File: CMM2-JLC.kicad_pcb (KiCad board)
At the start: 4 copper layers, 130 x 102 mm, 112 parts, among them J1 Nunchuck, J2 VGA, J3 EXTERNAL I/O, J4 USB_C_Receptacle_USB2.0, J5 Audio, J6 USB A Host, J7 SWD, J8 Micro_SD_Card_Det, J9 Boot select, SW1 Reset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

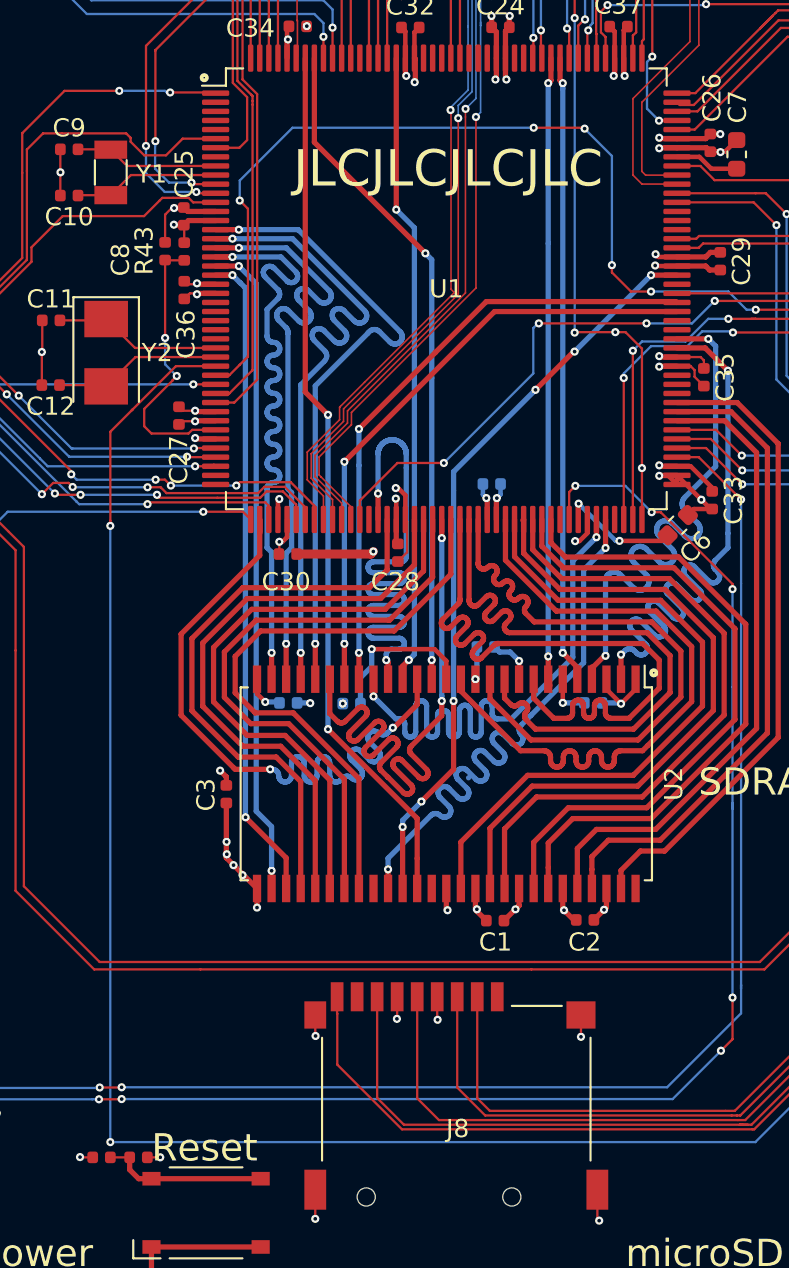
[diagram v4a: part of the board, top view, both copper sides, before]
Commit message: Fix reversed SDRAM bank select and some style/DRC issues
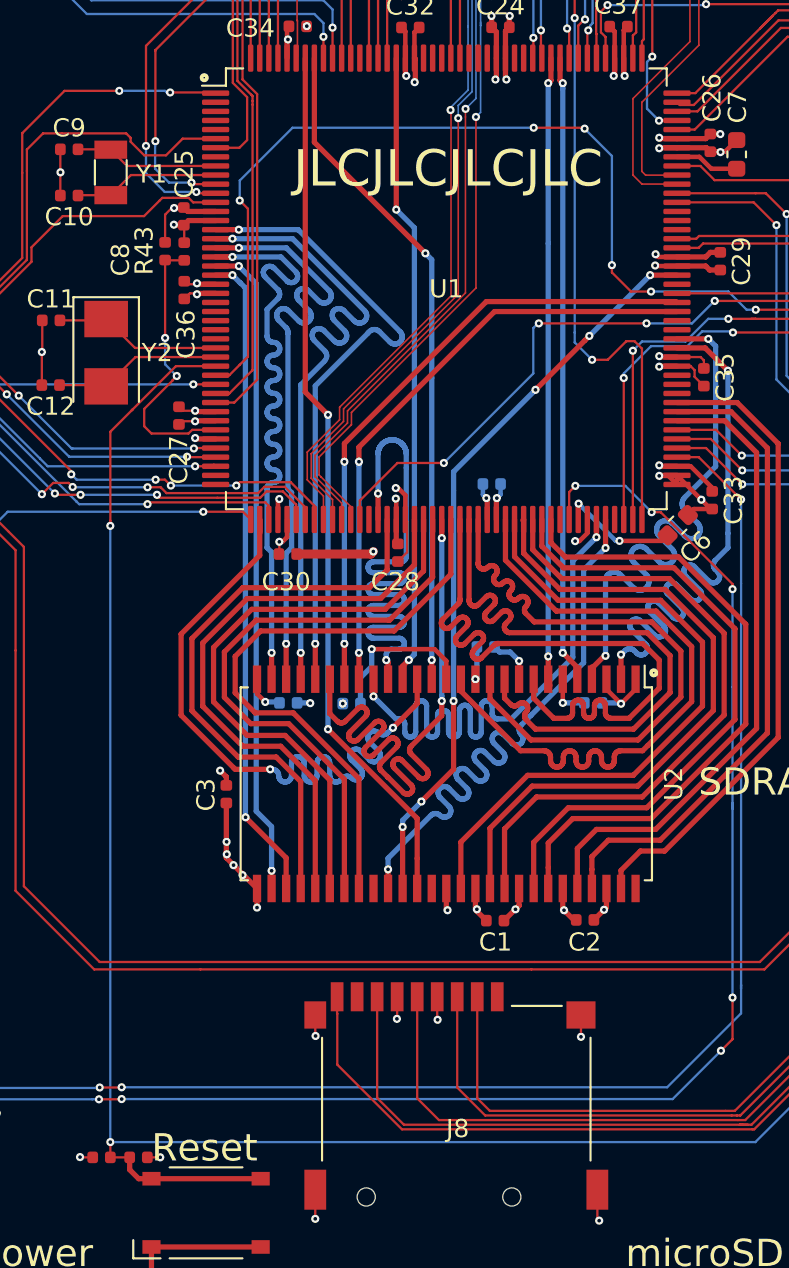
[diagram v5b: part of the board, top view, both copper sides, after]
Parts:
- removed REF**: OSHW-Logo_38.1x40mm_SilkScreen, Symbol:OSHW-Logo_38.1x40mm_SilkScreen
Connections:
- U2 pad 20: /PG5 -> /PG4
- U2 pad 21: /PG4 -> /PG5
- U3 pad 1: /USB_C_D+ -> /USB_C_D-
- U3 pad 3: /USB_C_D- -> /USB_C_D+
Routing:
- net /I2C2_SCL: track 61.4 -> 62.6 mm, vias 6 -> 4
- net /RESET: track 151.1 -> 151.9 mm

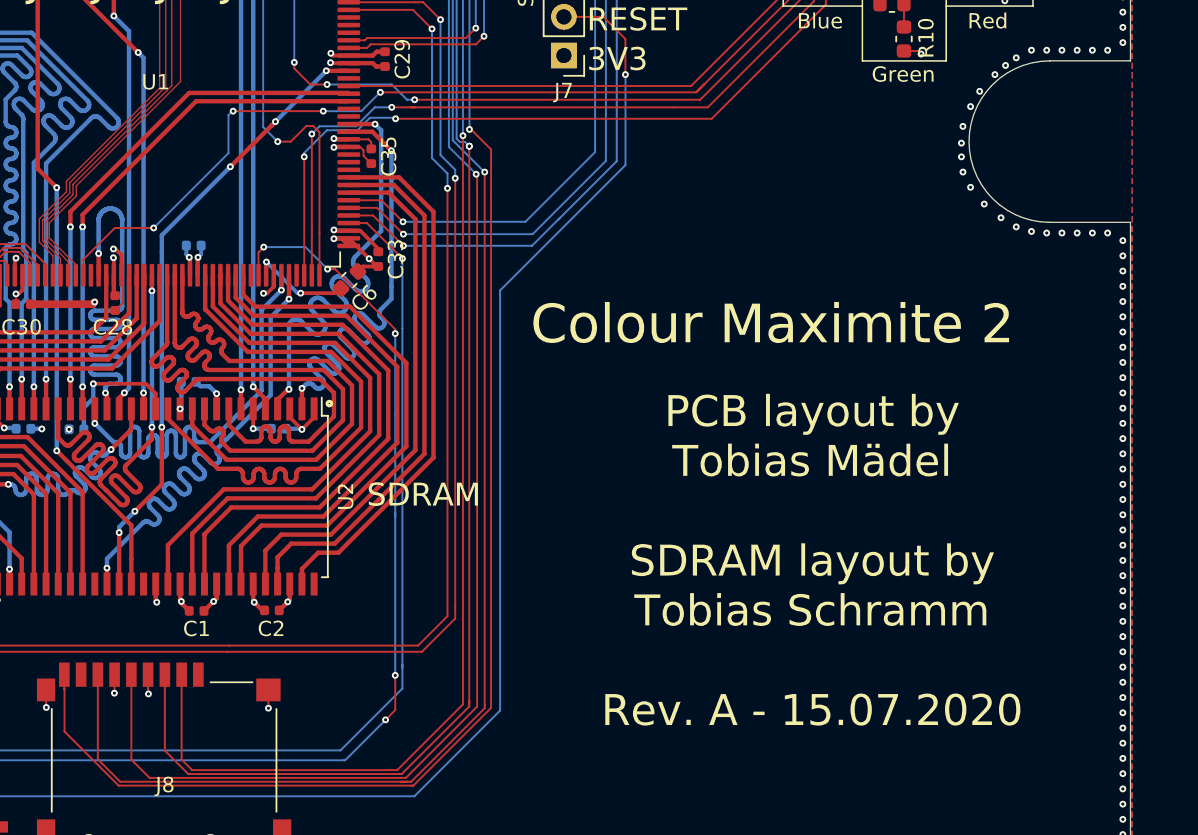
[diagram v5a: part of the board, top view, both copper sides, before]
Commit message: Rev B: Hook up SDRAM address line A12
The old sdram symbol did not fit the sdram used. This commit introduces a
new sdram symbol with address line A12 and bumps the revision to Rev B.
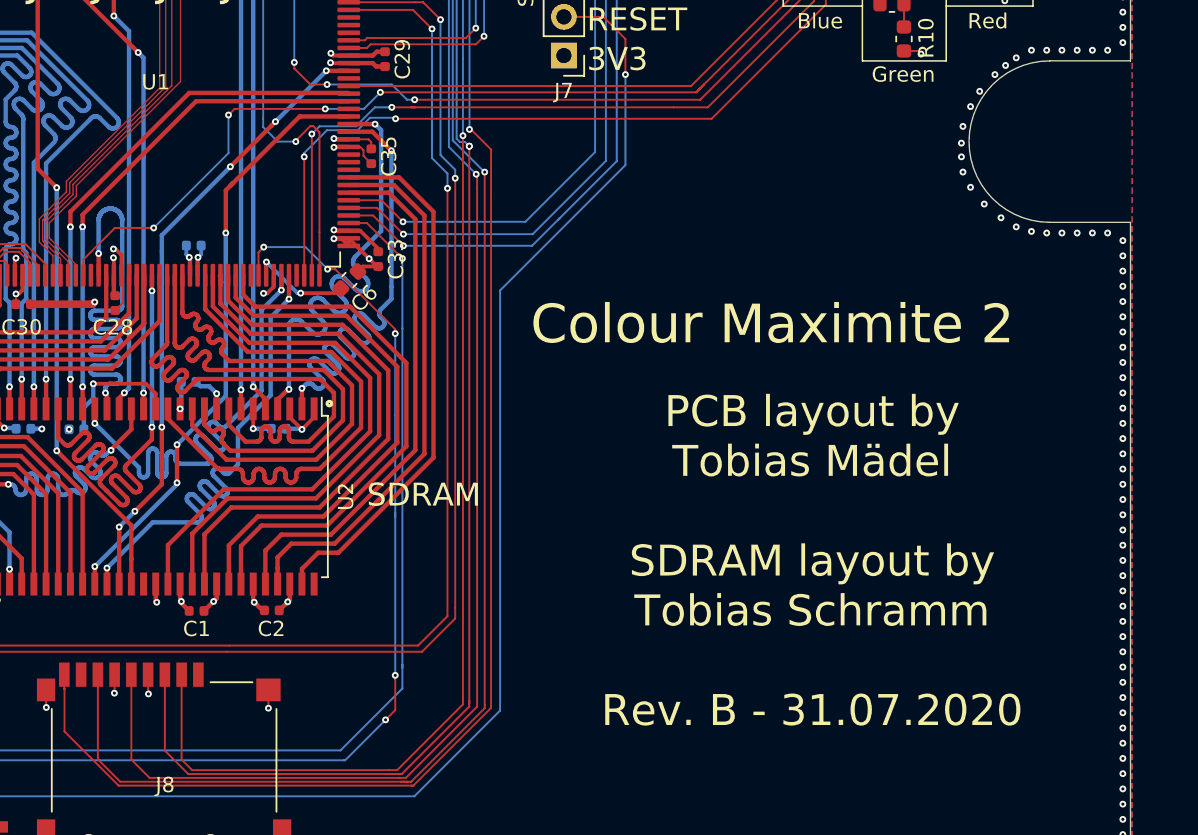
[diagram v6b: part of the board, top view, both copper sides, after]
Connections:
- U2 pad 36: (no net) -> /PG2
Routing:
- net /PG2: track 0.00 -> 39.7 mm, vias 0 -> 4
- net /PH6: track 34.1 -> 34.7 mm
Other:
- board text added: "PCB layout by Tobias Mädel SDRAM layout by Tobias Schramm Rev. B - 31.07.2020"
- board text removed: "PCB layout by Tobias Mädel SDRAM layout by Tobias Schramm Rev. A - 15.07.2020"
